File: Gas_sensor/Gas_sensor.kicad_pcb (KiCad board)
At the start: 4 copper layers, 44.6 x 100.2 mm, 143 parts, among them J1 Conn_02x02_Counter_Clockwise, J2 Conn_01x04, J3 Conn_01x10, J4 Conn_01x01, J5 Conn_01x01, Q1 DMC1229UFDB, Q2 DMC1229UFDB, Q3 Q_NMOS_GSD, Q4 Q_NMOS_GSD, Q5 Q_NMOS_GSD, Q6 Q_NMOS_GSD, SW1 SW_Push, SW10 SW_Push, SW11 SW_Push, SW12 SW_Push, SW2 SW_Push, SW3 SW_Push, SW4 SW_Push, SW5 SW_Push, SW6 SW_Push, SW7 SW_Push, SW8 SW_Push, SW9 SW_Push, U1 LPV511, U10 MCP1700-3302E_SOT23, U11 STM32F401CCUx, U12 TMP117, U13 TPS63070, U14 TPS79333-EP, U15 REG102GA, U2 LPV511, U3 MCP47CMB22, U4 MCP6V71, U5 LPV511, U6 MCP6V71, U7 MCP6V71, U8 MCP6V71, U9 ADS1115IDGS, Y1 25MHz

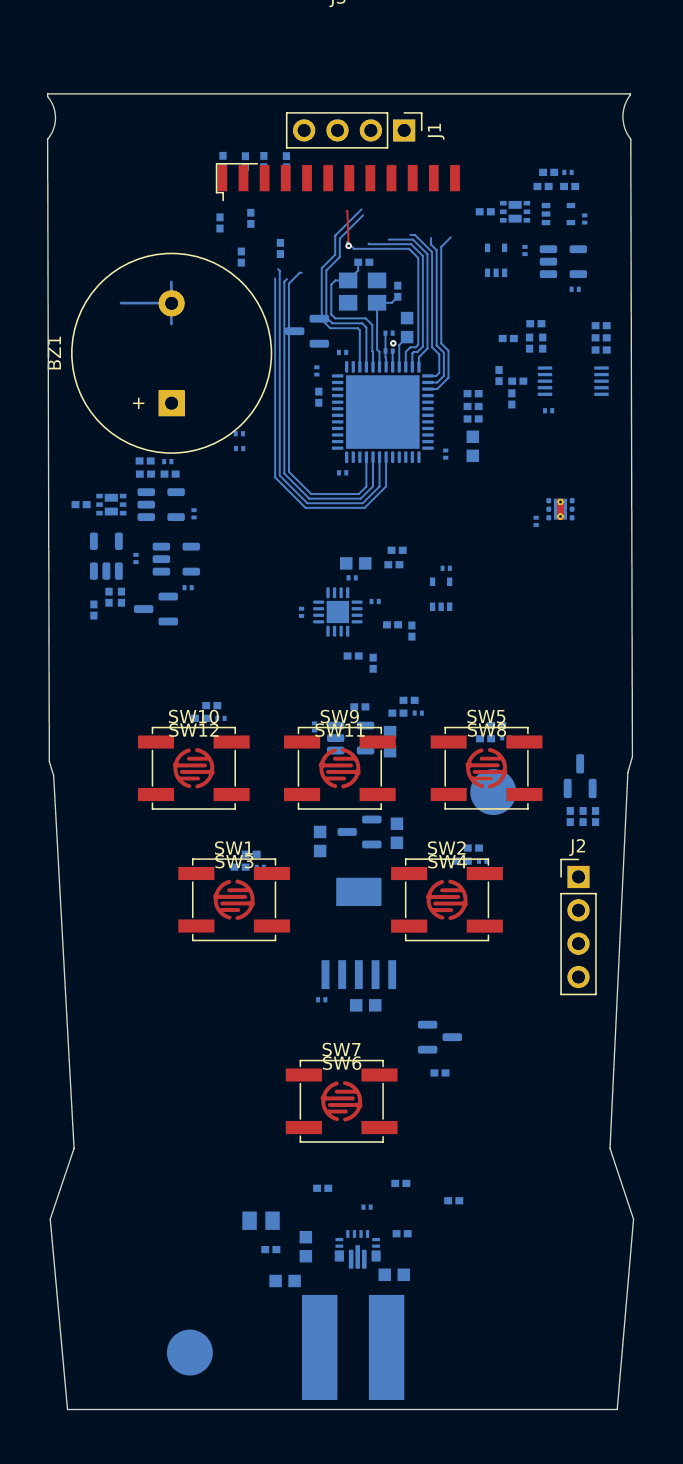
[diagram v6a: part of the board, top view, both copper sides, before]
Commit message: gas sensor : update layout
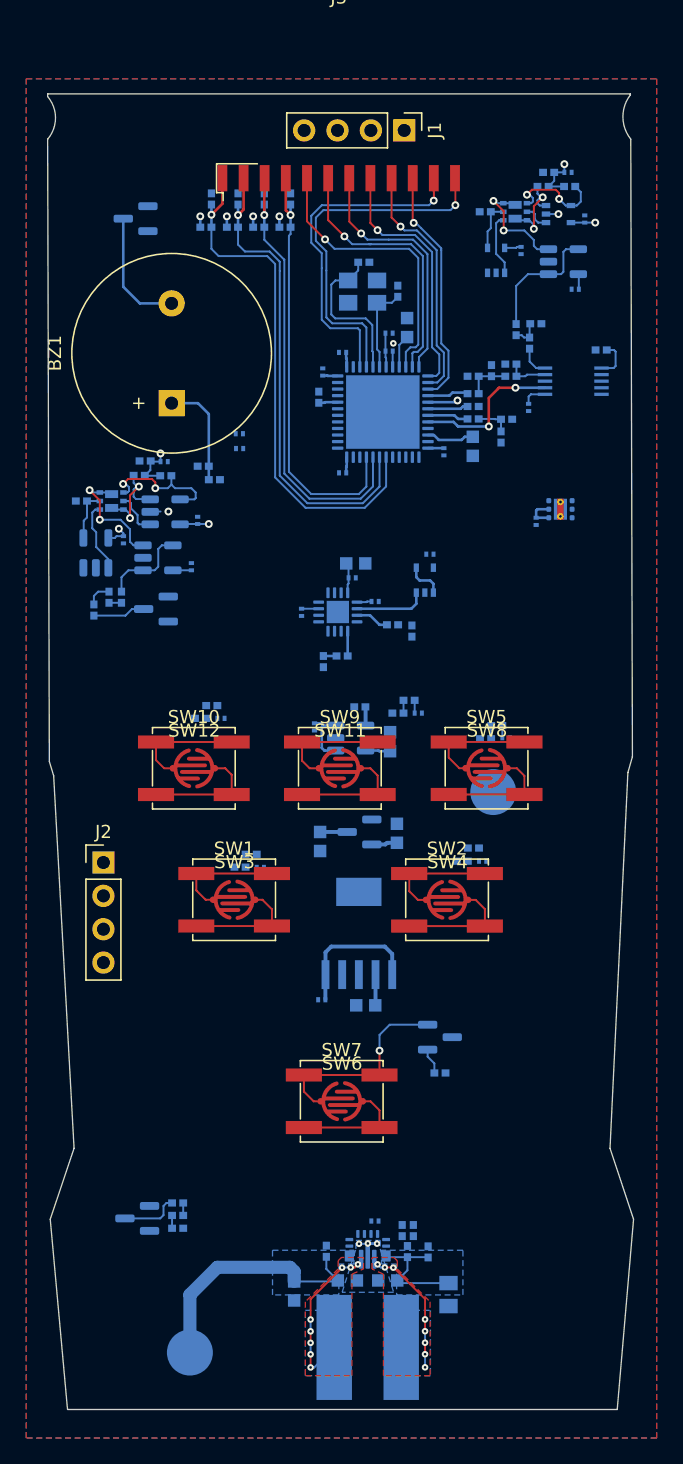
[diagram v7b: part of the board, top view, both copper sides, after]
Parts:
- moved Q5 47.7 mm to (40.5, 125.8), turned to 180 degrees
- moved R42 43.3 mm to (43.5, 124.6), turned to 180 degrees
- moved R40 43.3 mm to (43.5, 126.5), turned to 180 degrees
- moved R41 43.3 mm to (43.5, 125.5), turned to 0 degrees
- moved J2 36.2 mm to (37.9, 98.7)
- moved R20 16.1 mm to (45.5, 68.5), turned to 0 degrees
- moved Q4 15.6 mm to (40.3, 49.6)
- moved C40 15.3 mm to (64.2, 131.6), turned to -90 degrees
- moved R18 15.1 mm to (46.3, 69.5)
- moved R13 11.4 mm to (68.2, 66.3), turned to 90 degrees
- moved C18 9.50 mm to (68.6, 64.9)
- moved R55 9.38 mm to (62.6, 128.3), turned to 90 degrees
- moved R49 5.21 mm to (61.0, 128.3), turned to 90 degrees
- moved C46 4.74 mm to (56.5, 130.5)
- moved R51 4.53 mm to (60.6, 126.7), turned to 90 degrees
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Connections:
- R11 pad 1: /Vsensor -> /Vheater
- R12 pad 1: /Vheater -> /Vsensor
- R56 pad 2: Net-(R22-Pad2) -> Net-(R21-Pad2)
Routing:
- net GND: track 1.20 -> 59.3 mm, vias 1 -> 6
- net +BATT: track 0.00 -> 36.9 mm
- net /Vcomm2: track 0.00 -> 34.1 mm, vias 0 -> 1
- net /Buzzer_EN: track 31.0 -> 0.00 mm
- net +3V3: track 0.00 -> 29.1 mm, vias 0 -> 6
- net /Vseg7: track 0.00 -> 27.4 mm, vias 0 -> 1
- net /Vseg6: track 0.00 -> 25.8 mm, vias 0 -> 1
- net +9V: track 0.00 -> 18.7 mm, vias 0 -> 3
- net Net-(BZ1-Pad2): track 25.1 -> 9.39 mm
- net Net-(J5-Pad1): track 0.00 -> 15.6 mm, vias 0 -> 1
- net /Vcomm0: track 27.5 -> 40.5 mm, vias 0 -> 1
- net Net-(L1-Pad1): track 0.00 -> 12.3 mm, vias 0 -> 8
- net /~{RDY}: track 0.00 -> 11.6 mm, vias 0 -> 2
- net /Vcomm1: track 27.0 -> 37.3 mm, vias 0 -> 1
- net Net-(Q2-Pad4): track 0.00 -> 10.3 mm, vias 0 -> 2
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- added copper zone on B.Cu, net +9V
- added copper zone on B.Cu, net +BATT
- added copper zone on B.Cu, net GND
- added copper zone on F.Cu, net GND
- added copper zone on In1.Cu, net GND
- added copper zone on B.Cu, net Net-(L1-Pad1)
- added copper zone on F.Cu, net Net-(L1-Pad1)
- added copper zone on B.Cu, net Net-(L1-Pad2)
- added copper zone on F.Cu, net Net-(L1-Pad2)
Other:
- rule pad_to_mask_clearance: 0.1 -> 0.07

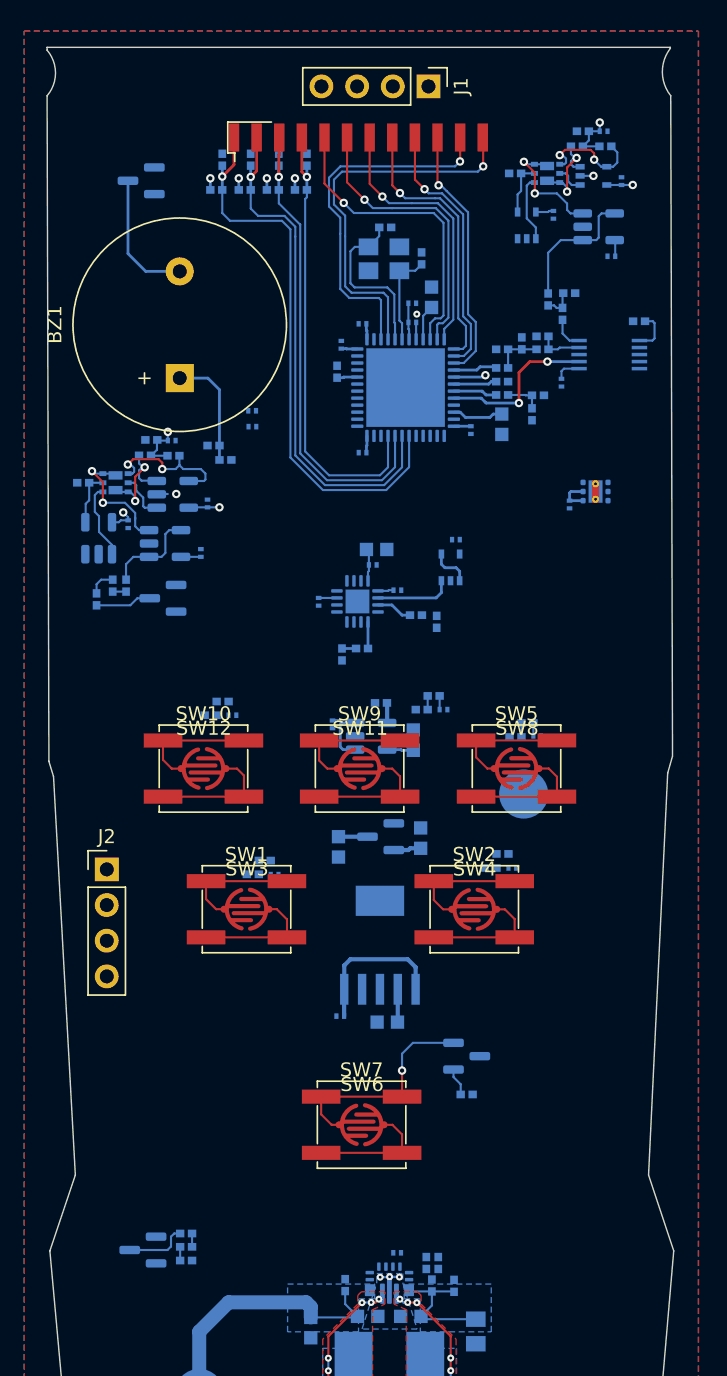
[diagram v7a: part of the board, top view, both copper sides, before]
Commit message: gas sensor : update layout
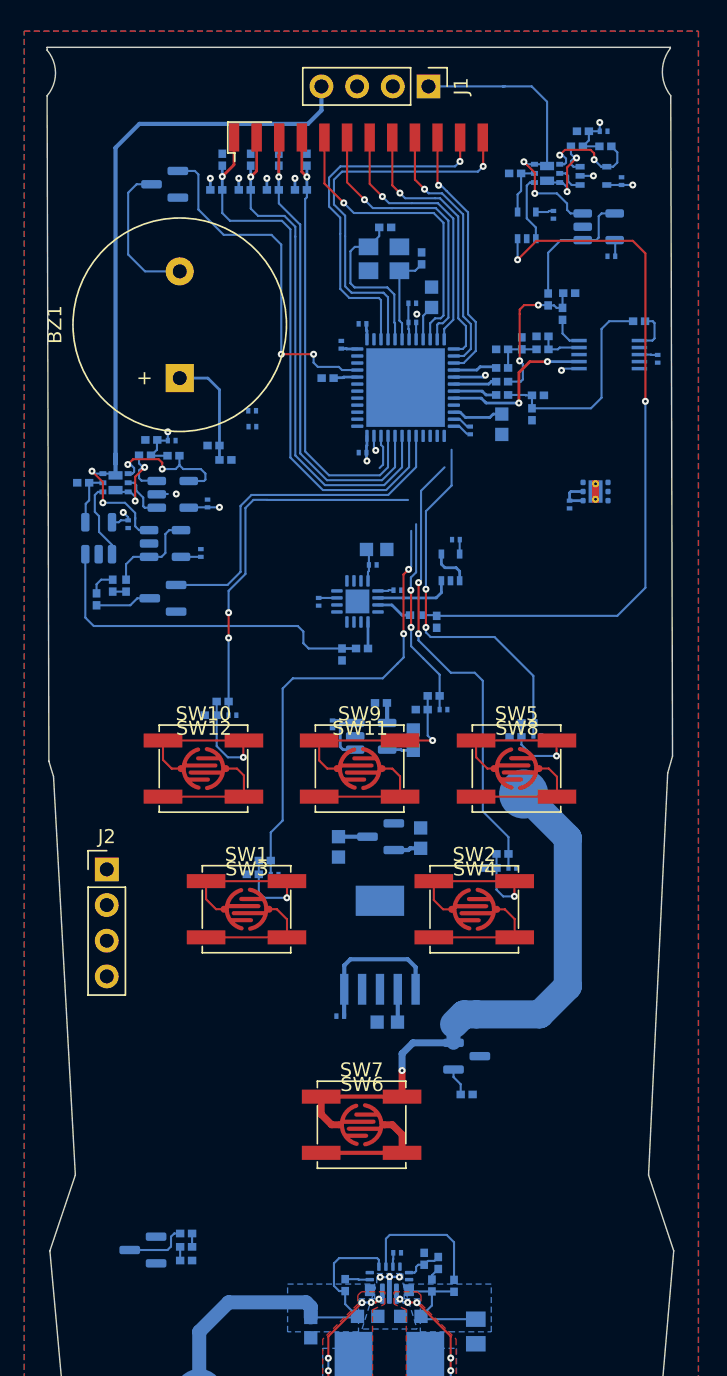
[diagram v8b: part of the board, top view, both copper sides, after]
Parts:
- moved C22 7.06 mm to (77.1, 62.3)
- moved Q4 1.69 mm to (42.0, 49.9)
- moved R25 0.81 mm to (53.6, 63.7), turned to 180 degrees
- moved R51 0.34 mm to (60.5, 126.4)
- moved C28 0.06 mm to (63.8, 67.4), turned to 90 degrees
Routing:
- net /Isensor: track 0.00 -> 52.1 mm, vias 0 -> 2
- net Net-(J1-Pad4): track 9.10 -> 50.6 mm
- net /Sound: track 0.00 -> 32.9 mm, vias 0 -> 2
- net /APO: track 0.00 -> 32.4 mm, vias 0 -> 2
- net /Low: track 0.00 -> 27.1 mm, vias 0 -> 2
- net /High: track 0.92 -> 27.0 mm, vias 0 -> 2
- net Net-(J5-Pad1): track 15.6 -> 41.2 mm
- net /Vheater_EN: track 0.00 -> 25.5 mm
- net /Buzzer_EN: track 0.00 -> 25.0 mm, vias 0 -> 2
- net /Iheater: track 1.00 -> 25.2 mm
- net Net-(J1-Pad1): track 8.61 -> 22.2 mm
- net /Mid: track 0.97 -> 14.2 mm, vias 0 -> 2
- net /ADC2: track 2.67 -> 15.3 mm
- net Net-(R55-Pad2): track 0.00 -> 9.84 mm
- net /ADC1: track 2.17 -> 10.5 mm, vias 0 -> 2
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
